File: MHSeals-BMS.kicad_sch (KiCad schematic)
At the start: 2 parts, among them U1 LM74800QDRRRQ1, U2 LM74800QDRRRQ1

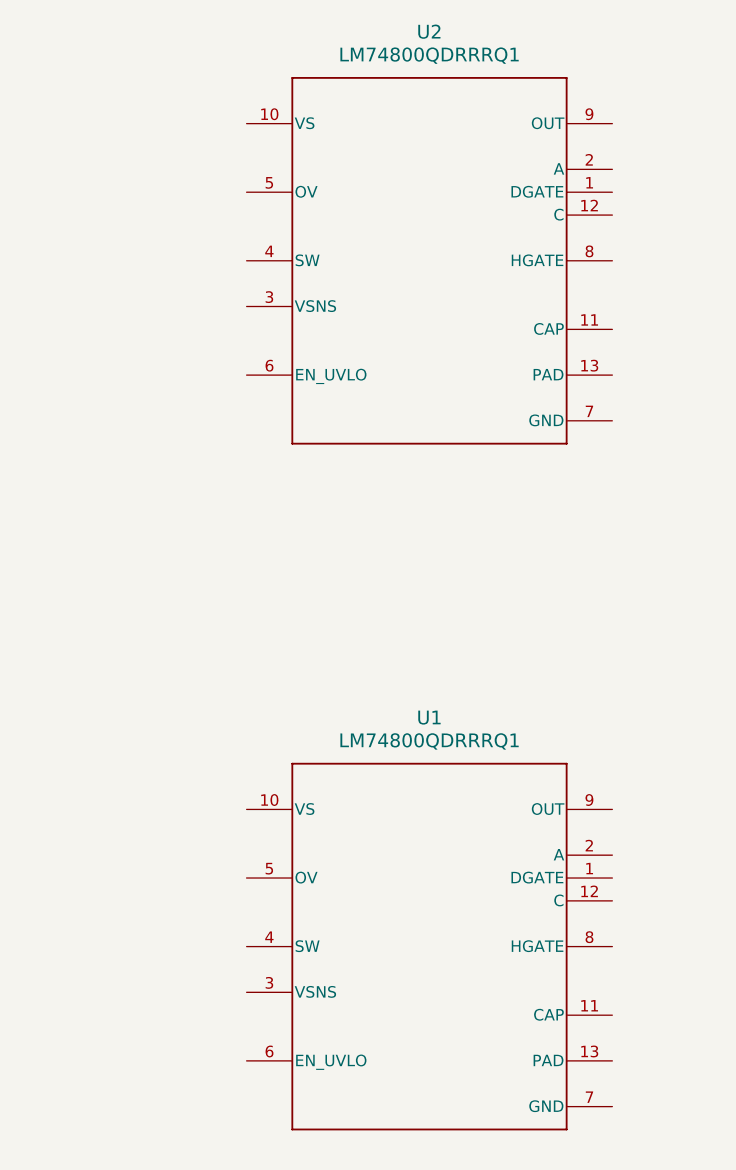
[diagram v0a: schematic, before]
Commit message: Changed placement of pins in symbol editor
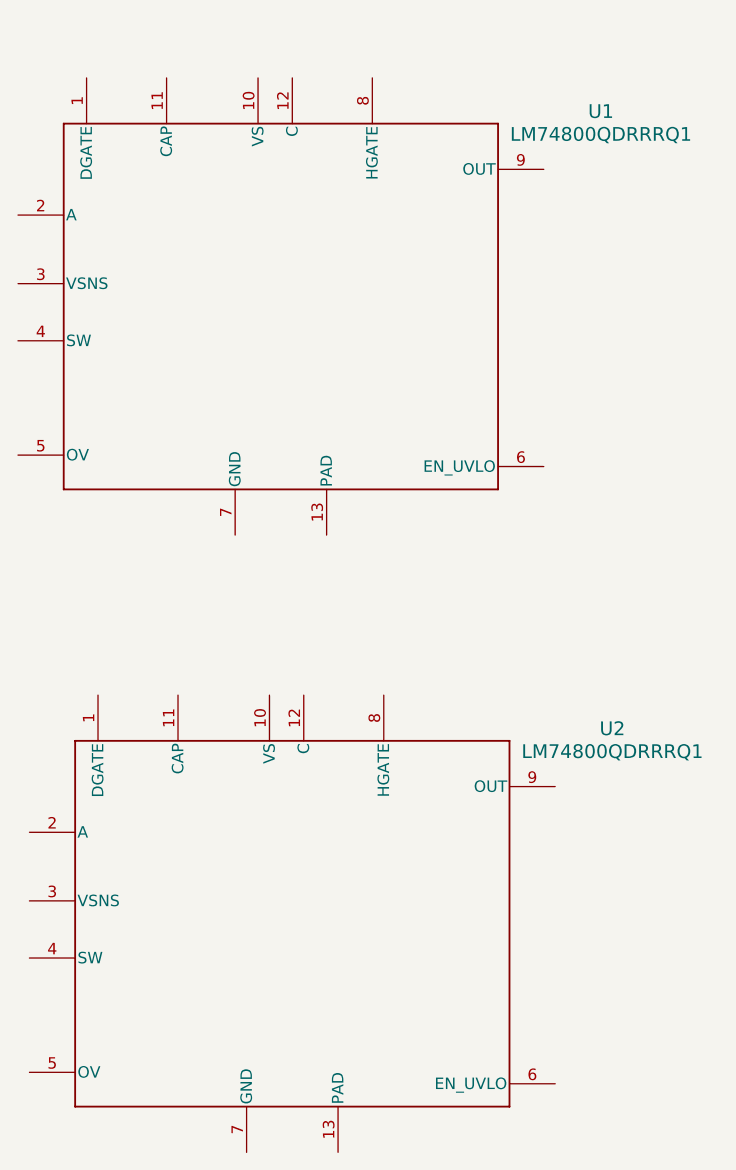
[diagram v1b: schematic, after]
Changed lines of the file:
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@@
 (kicad_sch
-	(version 20231120)
+	(version 20250114)
 	(generator "eeschema")
-	(generator_version "8.0")
+	(generator_version "9.0")
 	(paper "A4")
 	(symbol
 		(lib_id "2025-05-21_18-58-05:LM74800QDRRRQ1")
-		(at 137.16 62.23 0)
+		(at 120.65 67.31 0)
 		(unit 1)
 		(exclude_from_sim no)
@@
 		(dnp no)
 		(fields_autoplaced yes)
-		(property "Reference" "U2"
-			(at 137.16 36.83 0)
+		(property "Reference" "U1"
+			(at 156.21 45.6498 0)
 			(effects
 				(font
@@
 		)
 		(property "Value" "LM74800QDRRRQ1"
-			(at 137.16 39.37 0)
+			(at 156.21 48.1898 0)
 			(effects
 				(font
@@
 		)
 		(property "Footprint" "DRR0012E"
-			(at 137.16 62.23 0)
+			(at 120.904 68.072 0)
 			(effects
 				(font
@@
 		)
 		(property "Datasheet" "LM74800QDRRRQ1"
-			(at 137.16 62.23 0)
+			(at 120.904 68.072 0)
 			(effects
 				(font
@@
 		)
 		(property "Description" ""
-			(at 137.16 62.23 0)
+			(at 120.65 67.31 0)
 			(effects
 				(font
@@
 			)
 		)
+		(pin "9"
+		)
+		(pin "6"
+		)
 		(pin "4"
 		)
-		(pin "5"
+		(pin "7"
 		)
-		(pin "8"
+		(pin "12"
 		)
-		(pin "6"
+		(pin "1"
 		)
 		(pin "11"
@@
 		(pin "13"
 		)
-		(pin "1"
+		(pin "5"
+		)
+		(pin "3"
+		)
+		(pin "2"
+		)
+		(pin "10"
+		)
+		(pin "8"
+		)
+		(instances
+			(project ""
+				(path "/d0110039-a9ff-45f9-bcee-bd832f1a804d"
+					(reference "U1")
+					(unit 1)
+				)
+			)
+		)
+	)
+	(symbol
+		(lib_id "2025-05-21_18-58-05:LM74800QDRRRQ1")
+		(at 121.92 135.89 0)
+		(unit 1)
+		(exclude_from_sim no)
+		(in_bom yes)
+		(on_board yes)
+		(dnp no)
+		(fields_autoplaced yes)
+		(property "Reference" "U2"
+			(at 157.48 114.2298 0)
+			(effects
+				(font
+					(size 1.524 1.524)
+				)
+			)
+		)
+		(property "Value" "LM74800QDRRRQ1"
+			(at 157.48 116.7698 0)
+			(effects
+				(font
+					(size 1.524 1.524)
+				)
+			)
+		)
+		(property "Footprint" "DRR0012E"
+			(at 122.174 136.652 0)
+			(effects
+				(font
+					(size 1.27 1.27)
+					(italic yes)
+				)
+				(hide yes)
+			)
+		)
+		(property "Datasheet" "LM74800QDRRRQ1"
+			(at 122.174 136.652 0)
+			(effects
+				(font
+					(size 1.27 1.27)
+					(italic yes)
+				)
+				(hide yes)
+			)
+		)
+		(property "Description" ""
+			(at 121.92 135.89 0)
+			(effects
+				(font
+					(size 1.27 1.27)
+				)
+				(hide yes)
+			)
+		)
+		(pin "9"
+		)
+		(pin "6"
+		)
+		(pin "4"
+		)
+		(pin "7"
 		)
 		(pin "12"
 		)
-		(pin "10"
+		(pin "1"
+		)
+		(pin "11"
+		)
+		(pin "13"
+		)
+		(pin "5"
 		)
 		(pin "3"
 		)
-		(pin "9"
+		(pin "2"
 		)
-		(pin "7"
+		(pin "10"
 		)
-		(pin "2"
+		(pin "8"
 		)
 		(instances
@@
 		)
 	)
-	(symbol
-		(lib_id "2025-05-21_18-58-05:LM74800QDRRRQ1")
-		(at 137.16 138.43 0)
-		(unit 1)
-		(exclude_from_sim no)
-		(in_bom yes)
-		(on_board yes)
-		(dnp no)
-		(fields_autoplaced yes)
-		(property "Reference" "U1"
-			(at 137.16 113.03 0)
-			(effects
-				(font
-					(size 1.524 1.524)
-				)
-			)
-		)
-		(property "Value" "LM74800QDRRRQ1"
-			(at 137.16 115.57 0)
-			(effects
-				(font
-					(size 1.524 1.524)
-				)
-			)
-		)
-		(property "Footprint" "DRR0012E"
-			(at 137.16 138.43 0)
-			(effects
-				(font
-					(size 1.27 1.27)
-					(italic yes)
-				)
-				(hide yes)
-			)
-		)
-		(property "Datasheet" "LM74800QDRRRQ1"
-			(at 137.16 138.43 0)
-			(effects
-				(font
-					(size 1.27 1.27)
-					(italic yes)
-				)
-				(hide yes)
-			)
-		)
-		(property "Description" ""
-			(at 137.16 138.43 0)
-			(effects
-				(font
-					(size 1.27 1.27)
-				)
-				(hide yes)
-			)
-		)
-		(pin "4"
-		)
-		(pin "5"
-		)
-		(pin "8"
-		)
-		(pin "6"
-		)
-		(pin "11"
-		)
-		(pin "13"
-		)
-		(pin "1"
-		)
-		(pin "12"
-		)
-		(pin "10"
-		)
-		(pin "3"
-		)
-		(pin "9"
-		)
-		(pin "7"
-		)
-		(pin "2"
-		)
-		(instances
-			(project ""
-				(path "/d0110039-a9ff-45f9-bcee-bd832f1a804d"
-					(reference "U1")
-					(unit 1)
-				)
-			)
-		)
-	)
 	(sheet_instances
 		(path "/"
@@
 		)
 	)
+	(embedded_fonts no)
 )

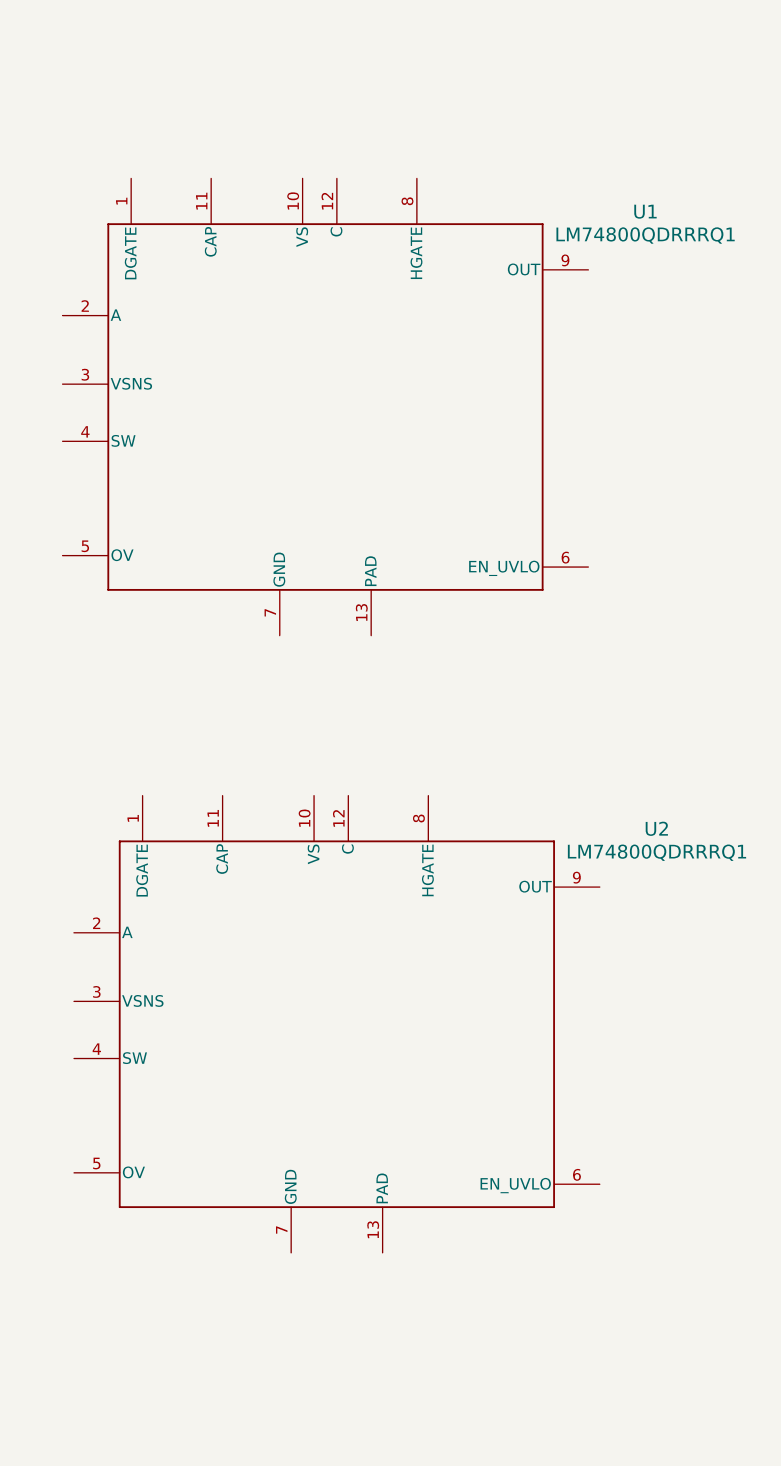
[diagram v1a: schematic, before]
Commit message: Updated schematic and symbols
Changed placement of EN/UVLO because reading datasheet of where it connects didn't match the schematic.
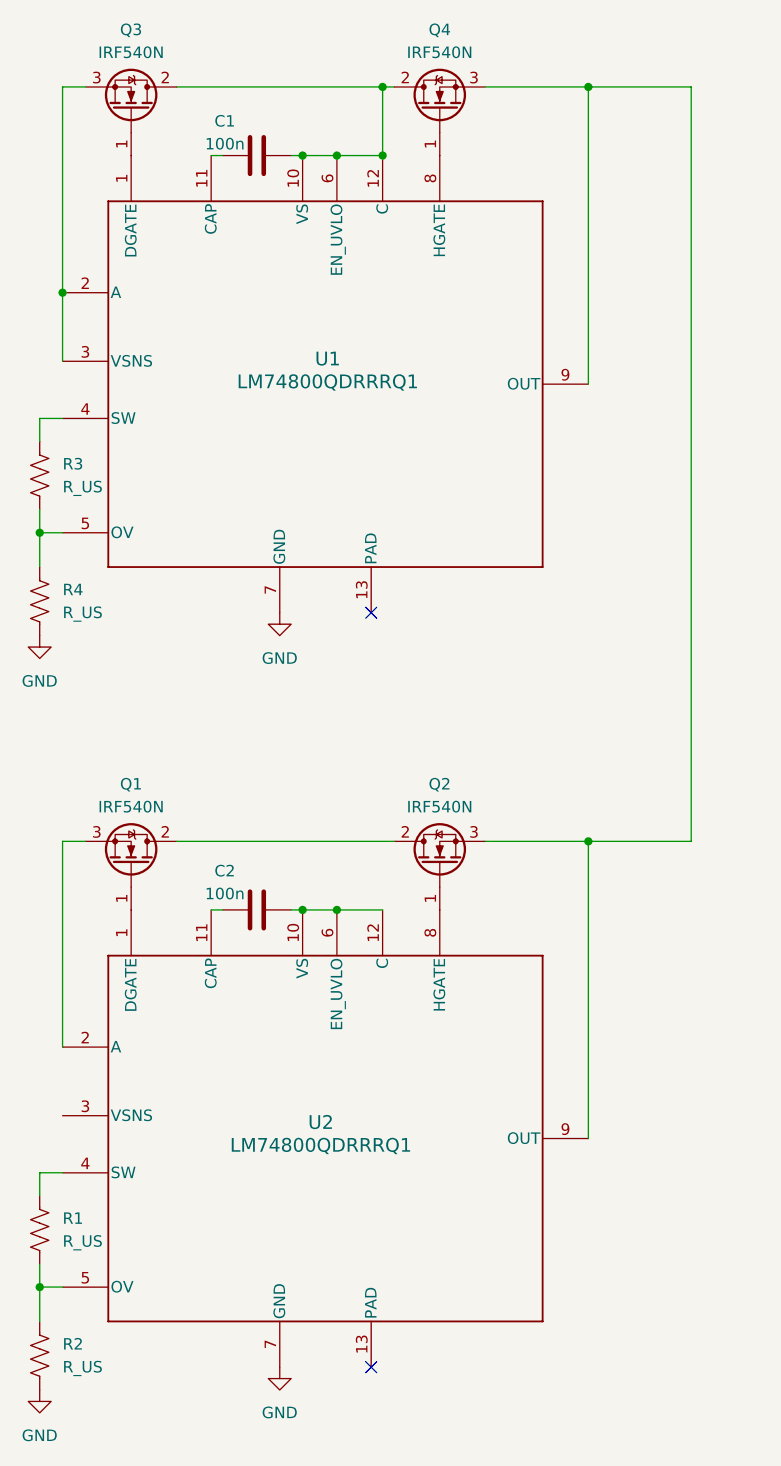
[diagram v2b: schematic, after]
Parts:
- added C1, C2: 100n, symbol Device:C
- added Q1, Q2, Q3, Q4: IRF540N, Package_TO_SOT_THT:TO-220-3_Vertical, symbol Transistor_FET:IRF540N
- added R1, R2, R3, R4: R_US, symbol Device:R_US
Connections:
- net at U1.1 (DGATE): now also Q3.1 (G)
- net at U1.10 (VS): now also U1.12 (C), U1.6 (EN_UVLO), C1.2, Q3.2 (D), Q4.2 (D)
- net at U1.11 (CAP): now also C1.1
- net at U1.2 (A): now also U1.3 (VSNS), Q3.3 (S)
- net at U1.4 (SW): now also R3.1
- net at U1.5 (OV): now also R3.2, R4.1
- net GND: now reaches U1.7 (GND)
- net GND: now also U2.7 (GND), R2.2, R4.2
- net at U1.8 (HGATE): now also Q4.1 (G)
- net at U1.9 (OUT): now also U2.9 (OUT), Q2.3 (S), Q4.3 (S)
- net at U2.1 (DGATE): now also Q1.1 (G)
- net at U2.10 (VS): now also U2.12 (C), U2.6 (EN_UVLO), C2.2
- net at U2.11 (CAP): now also C2.1
- net at U2.2 (A): now also Q1.3 (S)
- net at U2.4 (SW): now also R1.1
- net at U2.5 (OV): now also R1.2, R2.1
- net at U2.8 (HGATE): now also Q2.1 (G)
- new net: Q1.2 (D), Q2.2 (D)
- no-connect marks 0 -> 2
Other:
- moved on the sheet: U1, U2

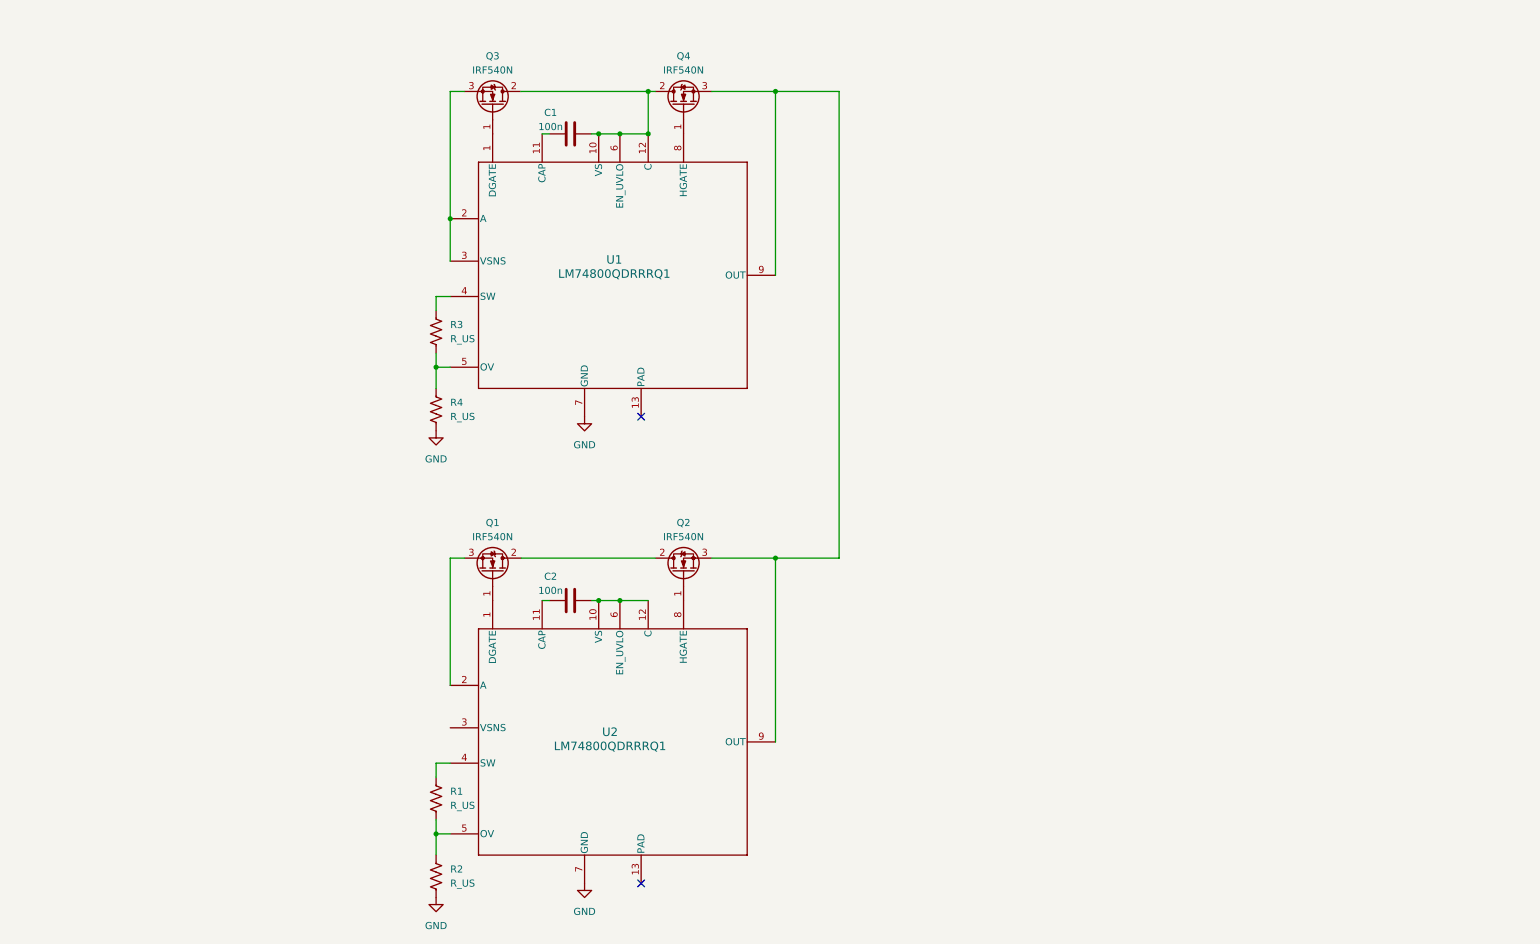
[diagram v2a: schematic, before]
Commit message: updating schematic with new version with BMS
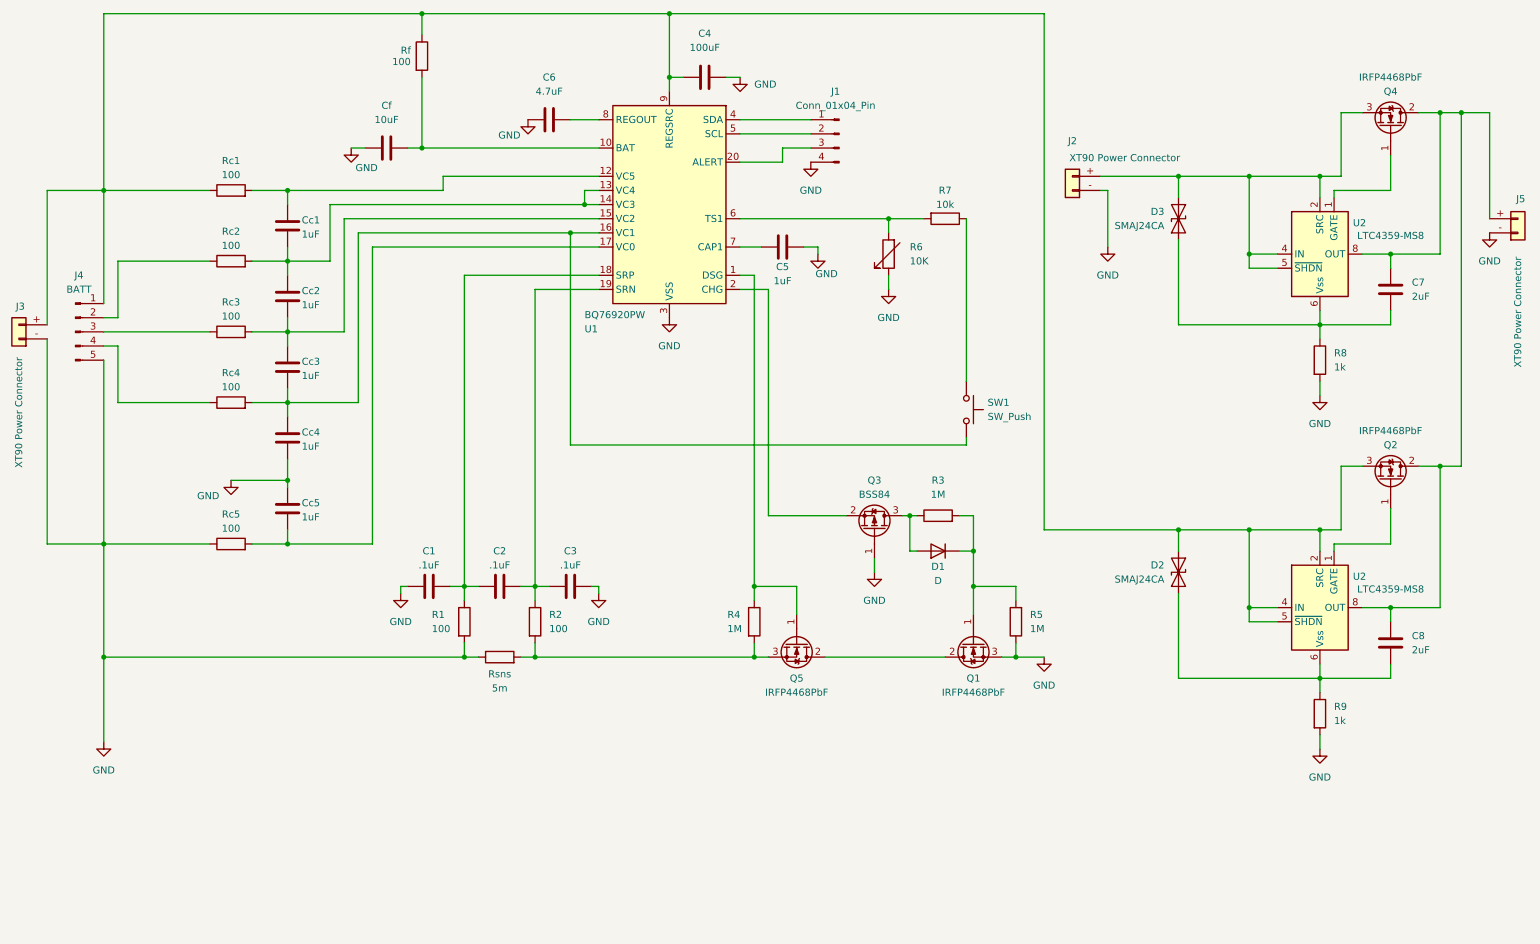
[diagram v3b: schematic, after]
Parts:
- removed Q1, Q2, Q3, Q4: IRF540N, Package_TO_SOT_THT:TO-220-3_Vertical, symbol Transistor_FET:IRF540N
- removed R1, R2, R3, R4: R_US, symbol Device:R_US
- removed U1, U2: LM74800QDRRRQ1, DRR0012E, symbol 2025-05-21_18-58-05:LM74800QDRRRQ1
- added C3: .1uF, symbol Device:C
- added C4: 100uF, symbol Device:C
- added C5, Cc1, Cc2, Cc3, Cc4, Cc5: 1uF, symbol Device:C
- added C6: 4.7uF, symbol Device:C
- added C7, C8: 2uF, symbol Device:C
- added Cf: 10uF, symbol Device:C
- added D1: D, symbol Device:D
- added D2, D3: SMAJ24CA, Diode_SMD:D_SMA, symbol Diode:SMAJ24CA
- added J1: Conn_01x04_Pin, symbol Connector:Conn_01x04_Pin
- added J2, J3, J5: XT90 Power Connector, symbol Connector_Generic:Conn_01x02
- added J4: BATT, symbol Connector:Conn_01x05_Pin
- added Q1, Q2, Q4, Q5: IRFP4468PbF, Package_TO_SOT_THT:TO-247-3_Vertical, symbol Transistor_FET:IRFP4468PbF
- added Q3: BSS84, Package_TO_SOT_SMD:SOT-23, symbol Transistor_FET:BSS84
- added R1, R2, Rc1, Rc2, Rc3, Rc4, Rc5, Rf: 100, symbol Device:R
- added R3, R4, R5: 1M, symbol Device:R
- added R6: 10K, symbol Device:R_Variable
- added R7: 10k, symbol Device:R
- added R8, R9: 1k, symbol Device:R
- added Rsns: 5m, symbol Device:R
- added SW1: SW_Push, symbol Switch:SW_Push
- added U1: BQ76920PW, Package_SO:TSSOP-20_4.4x6.5mm_P0.65mm, symbol Battery_Management:BQ76920PW
- added U2 (x2): LTC4359-MS8, Package_SO:MSOP-8_3x3mm_P0.65mm, symbol Power_Management:LTC4359-MS8
- C1, C2: value 100n -> .1uF
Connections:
- net GND: now also C1.1, C3.2, C4.2, C5.2, C6.1, Cc4.2, Cc5.1, Cf.1, J1.4 (Pin_4), J2.- (Pin_1), J3.- (Pin_1), J4.5 (Pin_5), J5.- (Pin_1), Q1.3 (S), Q3.1 (G), R1.2, R5.1, R6.1, R8.2, R9.2, Rc5.1, Rsns.1, U1.3 (VSS)
- net at C1.2: now also C2.1, R1.1, U1.18 (SRP)
- net at C2.2: now also C3.1, R2.1, U1.19 (SRN)
- new net: J4.2 (Pin_2), Rc2.1
- new net: Cc1.2, Cc2.1, Rc2.2, U1.13 (VC4), U1.14 (VC3)
- new net: Q5.1 (G), R4.1, U1.1 (DSG)
- new net: Cf.2, Rf.2, U1.10 (BAT)
- new net: Cc1.1, Rc1.2, U1.12 (VC5)
- new net: Cc2.2, Cc3.1, Rc3.2, U1.15 (VC2)
- new net: Cc3.2, Cc4.1, Rc4.2, SW1.2, U1.16 (VC1)
- new net: Cc5.2, Rc5.2, U1.17 (VC0)
- new net: Q3.2 (S), U1.2 (CHG)
- new net: J1.3 (Pin_3), U1.20 (ALERT)
- new net: J1.1 (Pin_1), U1.4 (SDA)
- new net: J1.2 (Pin_2), U1.5 (SCL)
- new net: R6.2, R7.2, U1.6 (TS1)
- new net: C5.1, U1.7 (CAP1)
- new net: C6.2, U1.8 (REGOUT)
- new net: C4.1, D2.1 (A1), J3.+ (Pin_2), J4.1 (Pin_1), Q2.3 (S), Rc1.1, Rf.1, U1.9 (REGSRC), U2.2 (SRC), U2.4 (IN), U2.5 (~{SHDN})
- new net: Q5.3 (S), R2.2, R4.2, Rsns.2
- new net: Q4.1 (G), U2.1 (GATE)
- new net: C7.1, C8.1, J5.+ (Pin_2), Q2.2 (D), Q4.2 (D), U2.8 (OUT), U2.8 (OUT)
- new net: D3.1 (A1), J2.+ (Pin_2), Q4.3 (S), U2.2 (SRC), U2.4 (IN), U2.5 (~{SHDN})
- new net: C8.2, D2.2 (A2), R9.1, U2.6 (Vss)
- new net: C7.2, D3.2 (A2), R8.1, U2.6 (Vss)
- new net: D1.2 (A), Q3.3 (D), R3.1
- new net: D1.1 (K), Q1.1 (G), R3.2, R5.2
- new net: Q1.2 (D), Q5.2 (D)
- new net: Q2.1 (G), U2.1 (GATE)
- new net: R7.1, SW1.1
- new net: J4.3 (Pin_3), Rc3.1
- new net: J4.4 (Pin_4), Rc4.1
- no-connect marks 2 -> 0
